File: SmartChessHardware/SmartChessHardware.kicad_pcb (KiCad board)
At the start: 2 copper layers, 294 parts, among them IC1 Pi-Zero-UART, IC2 Arduino_UNO_R3, IC3 MCP23017x-x-SO, J1 Barrel_Jack, SW200 SW_Reed, SW201 SW_Reed, SW202 SW_Reed, SW203 SW_Reed, SW204 SW_Reed, SW205 SW_Reed, SW206 SW_Reed, SW207 SW_Reed, SW208 SW_Reed, SW209 SW_Reed, SW210 SW_Reed, SW211 SW_Reed, SW212 SW_Reed, SW213 SW_Reed, SW214 SW_Reed, SW215 SW_Reed, SW216 SW_Reed, SW217 SW_Reed, SW218 SW_Reed, SW219 SW_Reed, SW220 SW_Reed, SW221 SW_Reed, SW222 SW_Reed, SW223 SW_Reed, SW224 SW_Reed, SW225 SW_Reed, SW226 SW_Reed, SW227 SW_Reed, SW228 SW_Reed, SW229 SW_Reed, SW230 SW_Reed, SW231 SW_Reed, SW232 SW_Reed, SW233 SW_Reed, SW234 SW_Reed, SW235 SW_Reed, SW236 SW_Reed, SW237 SW_Reed, SW238 SW_Reed, SW239 SW_Reed, SW240 SW_Reed, SW241 SW_Reed, SW242 SW_Reed, SW243 SW_Reed, SW244 SW_Reed, SW245 SW_Reed, SW246 SW_Reed, SW247 SW_Reed, SW248 SW_Reed, SW249 SW_Reed, SW250 SW_Reed, SW251 SW_Reed, SW252 SW_Reed, SW253 SW_Reed, SW254 SW_Reed, SW255 SW_Reed, SW256 SW_Reed, SW257 SW_Reed, SW258 SW_Reed, SW259 SW_Reed, SW260 SW_Reed, SW261 SW_Reed, SW262 SW_Reed, SW263 SW_Reed

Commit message: Placed board components
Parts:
- moved D108 368.0 mm to (302.1, 62.6)
- moved SW256 366.1 mm to (291.5, 252.5)
- moved SW216 361.2 mm to (292.0, 102.0)
- moved SW208 361.0 mm to (291.2, 72.0)
- moved D256 360.5 mm to (292.0, 260.5), turned to 90 degrees
- moved D208 360.1 mm to (291.5, 80.0), turned to 90 degrees
- moved D116 355.5 mm to (302.6, 92.2)
- moved SW240 352.2 mm to (292.5, 192.5)
- moved SW255 351.3 mm to (291.5, 222.5)
- moved SW224 351.2 mm to (293.0, 133.0)
- moved D216 350.0 mm to (292.0, 111.0), turned to 90 degrees
- moved D255 349.2 mm to (292.0, 230.5), turned to 90 degrees
- moved SW232 348.6 mm to (292.2, 164.0)
- moved D224 345.9 mm to (293.0, 139.5), turned to 90 degrees
- moved D232 344.8 mm to (292.5, 171.5), turned to 90 degrees
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
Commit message: Rearranged scanning groups
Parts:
- moved D239 211.3 mm to (293.3, 172.0)
- moved SW239 211.3 mm to (293.3, 163.5)
- moved D231 210.9 mm to (292.9, 140.1)
- moved SW231 210.9 mm to (292.4, 133.1)
- moved D223 210.2 mm to (293.2, 110.4)
- moved SW223 210.2 mm to (293.2, 102.4)
- moved D256 209.6 mm to (82.4, 261.0)
- moved SW256 209.6 mm to (81.9, 253.0)
- moved D247 209.6 mm to (293.1, 200.5)
- moved SW247 209.6 mm to (293.1, 192.5)
- moved D224 209.4 mm to (83.6, 139.9)
- moved SW224 209.4 mm to (83.6, 133.4)
- moved D263 209.2 mm to (292.2, 261.4)
- moved SW263 209.2 mm to (292.2, 252.9)
- moved D215 209.2 mm to (292.2, 82.0)
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
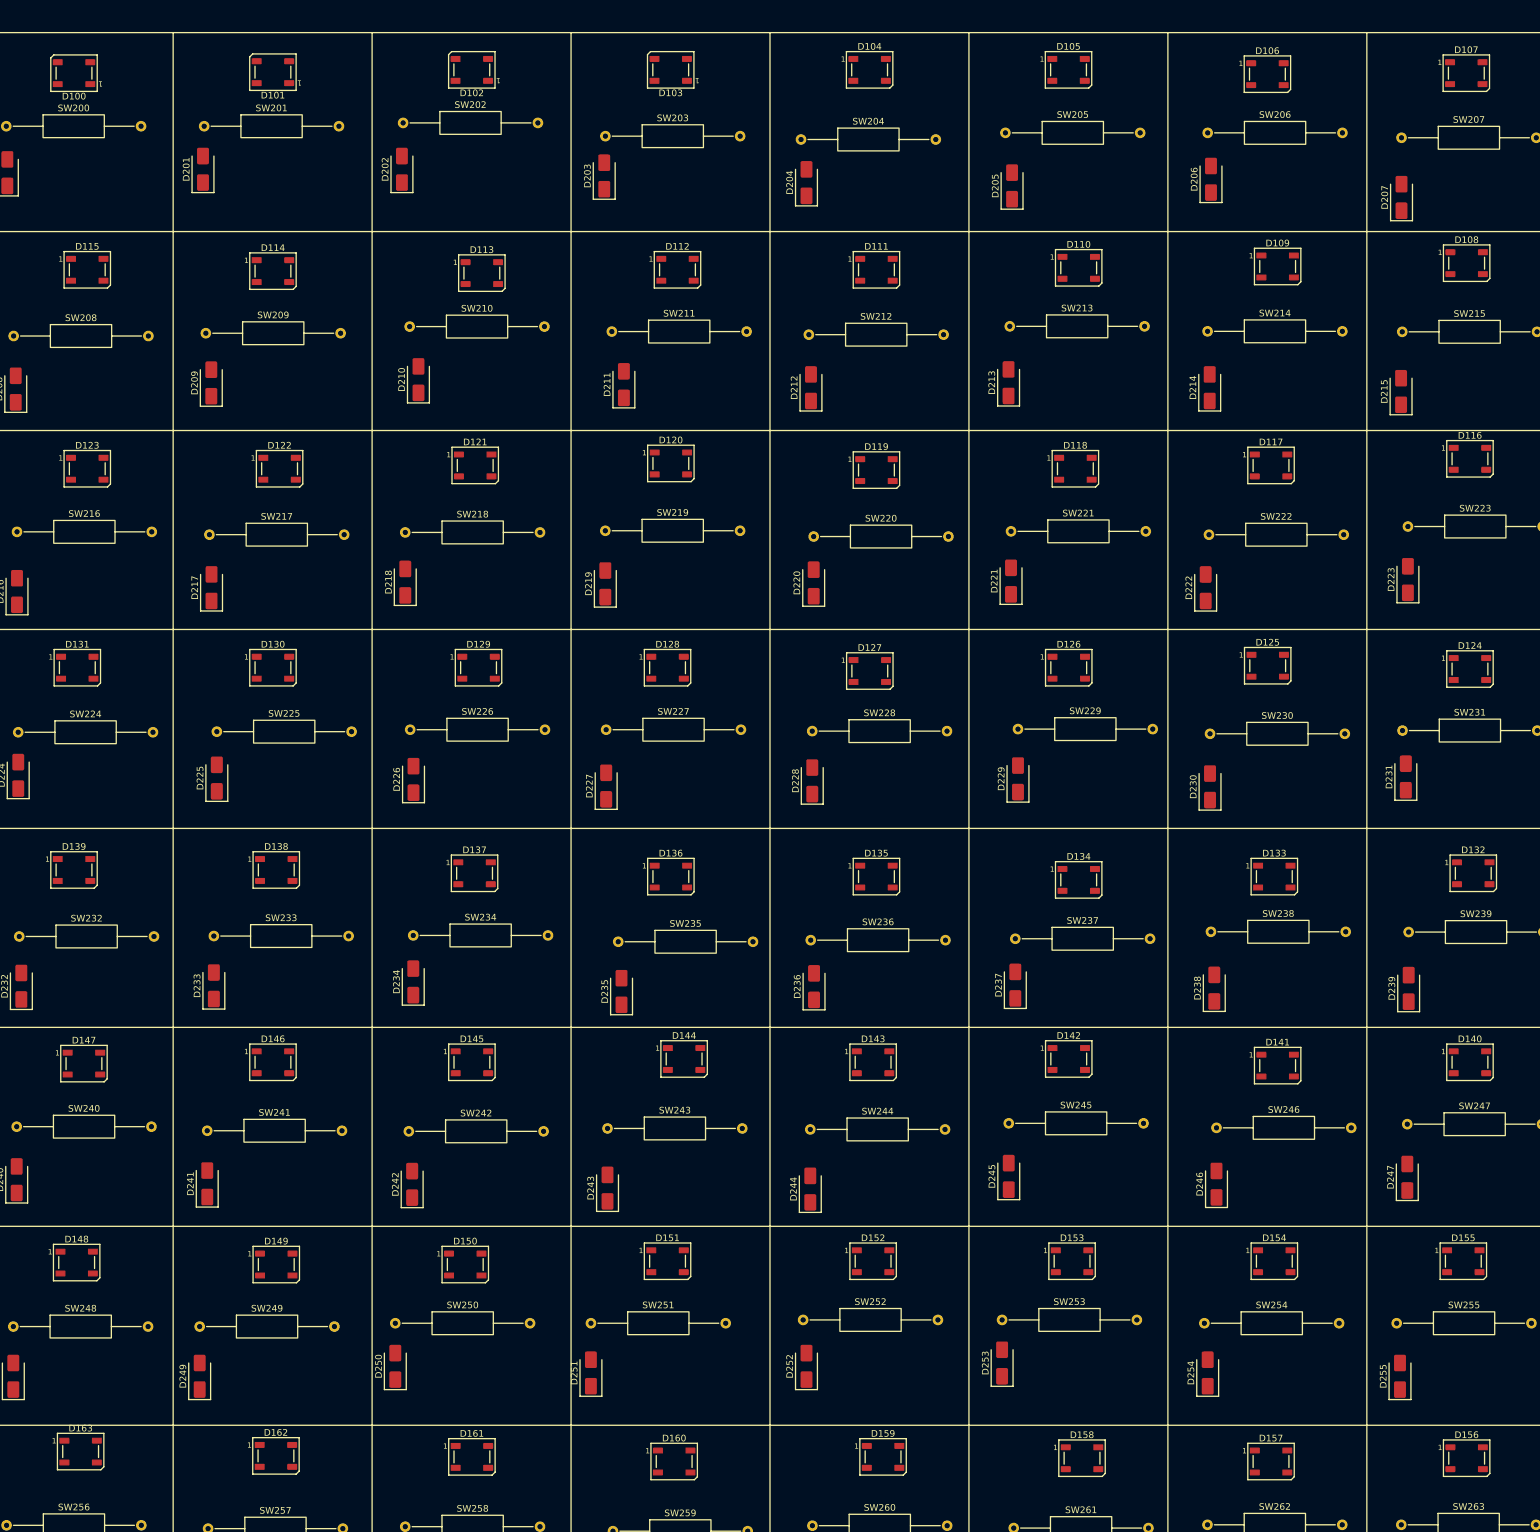
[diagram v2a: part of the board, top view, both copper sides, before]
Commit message: Fixed led placing
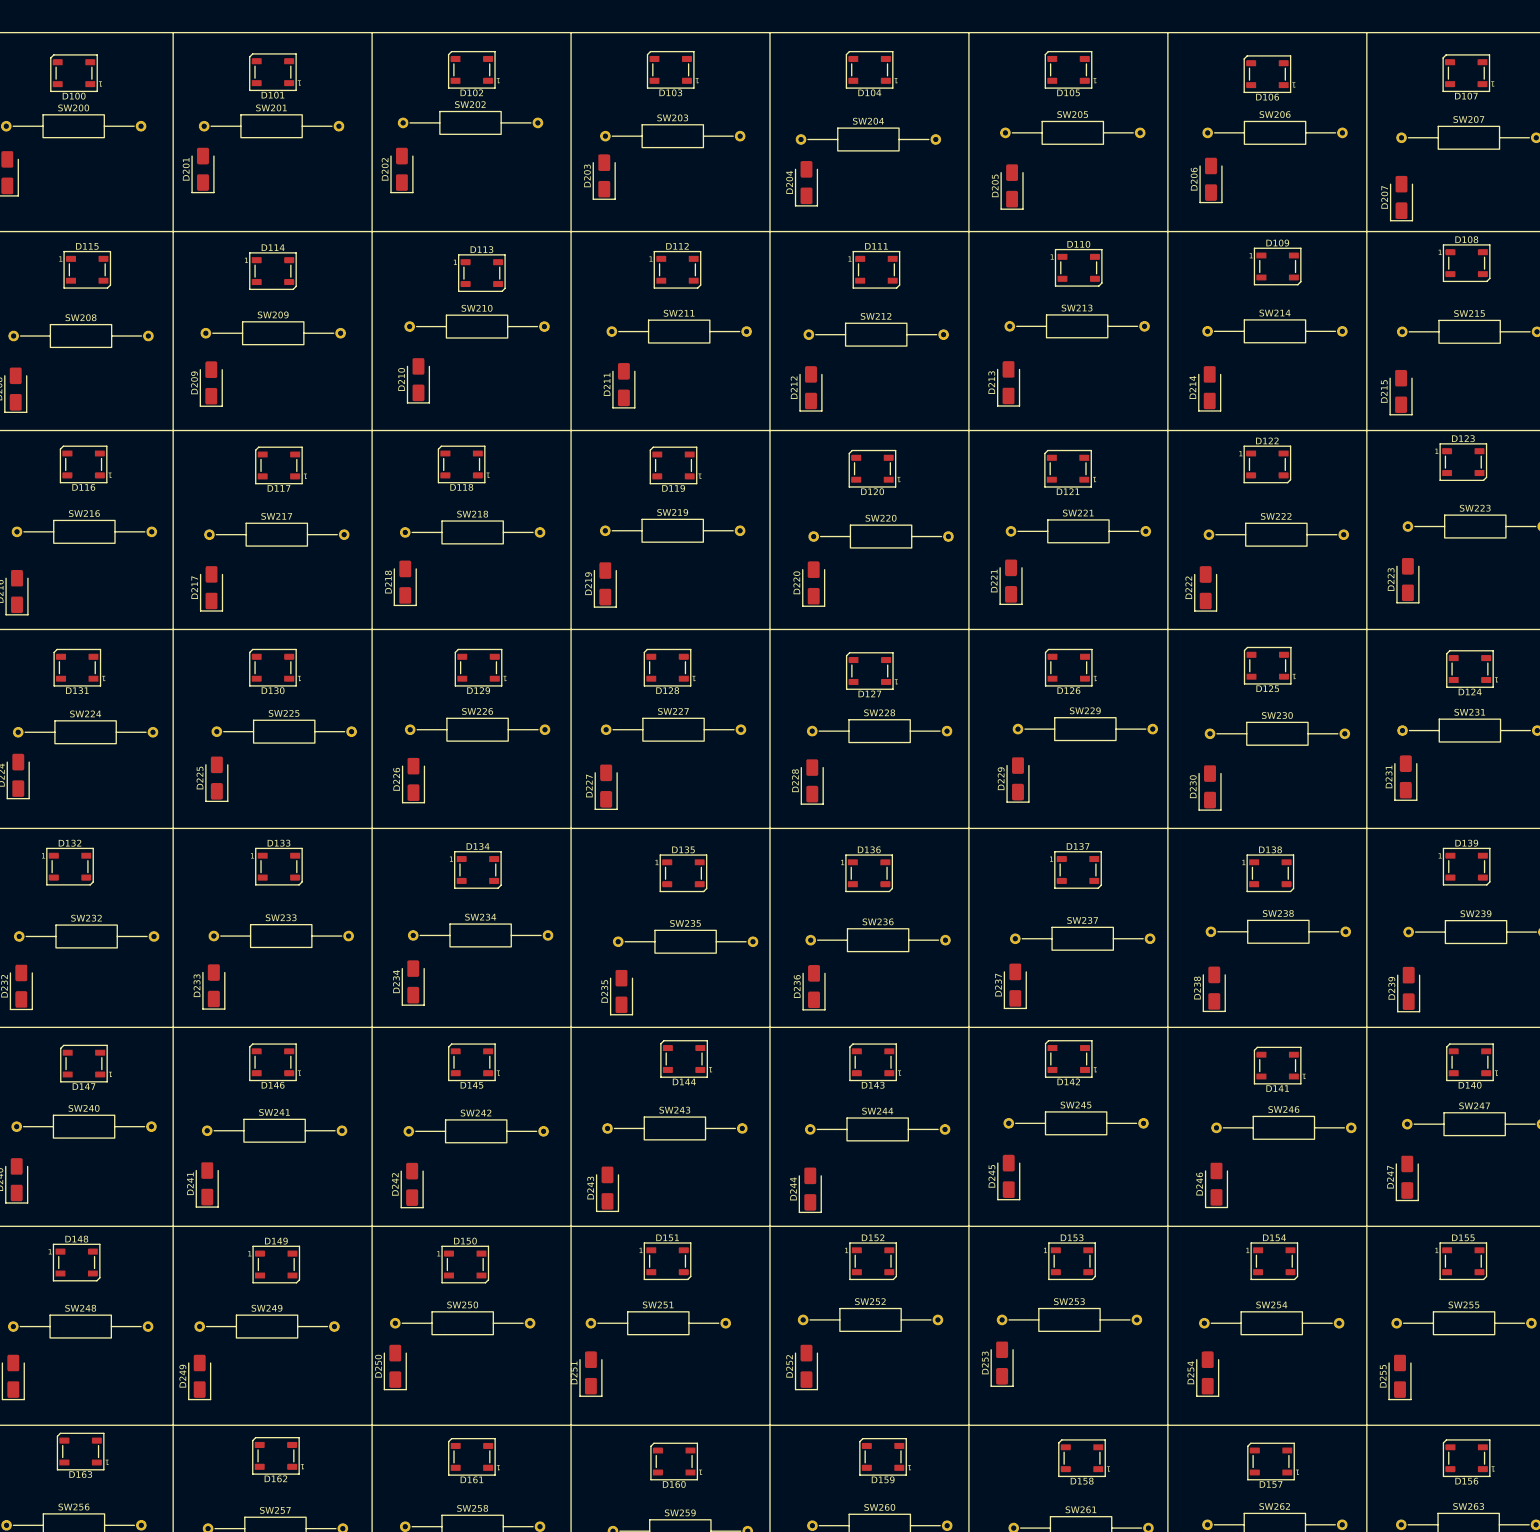
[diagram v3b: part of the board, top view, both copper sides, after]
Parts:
- moved D132 211.6 mm to (91.5, 153.7)
- moved D139 210.0 mm to (302.1, 153.7)
- moved D116 209.1 mm to (93.5, 93.0), turned to 180 degrees
- moved D123 207.5 mm to (301.6, 92.7)
- moved D133 150.1 mm to (123.0, 153.7)
- moved D138 149.9 mm to (272.4, 154.7)
- moved D117 149.6 mm to (123.0, 93.2), turned to 180 degrees
- moved D122 149.0 mm to (272.0, 93.0)
- moved D118 92.6 mm to (150.5, 93.0), turned to 180 degrees
- moved D137 91.0 mm to (243.4, 154.2)
- moved D134 90.6 mm to (152.9, 154.2)
- moved D121 89.4 mm to (241.9, 93.7), turned to 180 degrees
- moved D119 30.6 mm to (182.4, 93.2), turned to 180 degrees
- moved D120 30.4 mm to (212.4, 93.7), turned to 180 degrees
- moved D136 29.9 mm to (211.9, 154.7)
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
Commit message: Aligned LEDS
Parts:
- moved D135 2.65 mm to (181.7, 153.2)
- moved D118 2.64 mm to (152.9, 94.0)
- moved D109 2.38 mm to (271.3, 63.9)
- moved D110 2.05 mm to (241.6, 63.9)
- moved D137 1.81 mm to (241.9, 153.2)
- moved D158 1.73 mm to (242.3, 242.6)
- moved D150 1.63 mm to (152.2, 212.5)
- moved D108 1.62 mm to (301.0, 63.9)
- moved D134 1.61 mm to (151.6, 153.2)
- moved D159 1.57 mm to (212.5, 242.6)
- moved D154 1.52 mm to (271.7, 212.5)
- moved D138 1.49 mm to (272.0, 153.2)
- moved D133 1.47 mm to (121.5, 153.2)
- moved D136 1.42 mm to (211.8, 153.2)
- moved D146 1.37 mm to (123.4, 183.4)
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
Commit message: Aligned no key ghosting diodes
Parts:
- moved D216 4.68 mm to (83.1, 107.5)
- moved D262 4.42 mm to (262.5, 258.0)
- moved D222 4.10 mm to (262.9, 107.5)
- moved D217 4.10 mm to (113.1, 107.5)
- moved D207 3.74 mm to (292.2, 49.0)
- moved D219 3.60 mm to (173.0, 107.5)
- moved D220 3.43 mm to (203.0, 107.5)
- moved D218 3.41 mm to (143.0, 107.5)
- moved D263 3.40 mm to (292.5, 258.0)
- moved D235 3.38 mm to (173.0, 169.5)
- moved D260 3.31 mm to (202.6, 258.0)
- moved D261 3.14 mm to (232.5, 258.0)
- moved D221 3.12 mm to (232.9, 107.5)
- moved D211 3.03 mm to (172.7, 79.0)
- moved D215 3.00 mm to (292.0, 79.0)
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
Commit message: Placed Matrix pull up resistors
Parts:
- moved R207 336.4 mm to (311.5, 40.0)
- moved R206 306.5 mm to (281.5, 40.0)
- moved R205 276.9 mm to (251.8, 40.0)
- moved R204 246.8 mm to (221.7, 40.0)
- moved R203 216.9 mm to (191.5, 40.0)
- moved R202 187.3 mm to (161.5, 39.5)
- moved R201 157.5 mm to (131.5, 40.0)
- moved R200 135.9 mm to (101.3, 40.0)
- renumbered R207 to R200, R200 to R201, R201 to R202, R202 to R203, R203 to R204, R204 to R205, R205 to R206, R206 to R207

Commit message: Fixed wrong placed diodes
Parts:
- turned D124 to 0 degrees
- turned D125 to 0 degrees
- turned D126 to 0 degrees
- turned D127 to 0 degrees
- turned D128 to 0 degrees
- turned D129 to 0 degrees
- turned D130 to 0 degrees
- turned D131 to 0 degrees
- turned D132 to 180 degrees
- turned D133 to 180 degrees
- turned D134 to 180 degrees
- turned D135 to 180 degrees
- turned D136 to 180 degrees
- turned D137 to 180 degrees
- turned D138 to 180 degrees
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
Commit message: Placed filtering capacitors for leds
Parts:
- C114: footprint Capacitor_SMD:C_0603_1608Metric -> Capacitor_THT:CP_Radial_D6.3mm_P2.50mm; moved to B.Cu
- moved C106 410.3 mm to (306.5, 37.5), turned to 90 degrees
- moved C107 393.2 mm to (296.5, 60.0), turned to -90 degrees
- moved C105 382.1 mm to (276.5, 37.2), turned to 90 degrees
- moved C124 379.1 mm to (306.0, 96.5), turned to -90 degrees
- moved C108 367.1 mm to (267.0, 60.0), turned to -90 degrees
- moved C125 366.1 mm to (298.0, 121.5), turned to 90 degrees
- moved C139 365.9 mm to (306.5, 156.0), turned to 90 degrees
- moved C140 355.1 mm to (298.0, 181.0), turned to -90 degrees
- moved C156 354.9 mm to (306.0, 215.0), turned to -90 degrees
- moved C104 354.0 mm to (246.5, 37.5), turned to 90 degrees
- moved C123 350.0 mm to (276.5, 96.5), turned to -90 degrees
- moved C157 348.6 mm to (297.5, 240.0), turned to 90 degrees
- moved C109 341.0 mm to (237.0, 60.0), turned to -90 degrees
- moved C126 337.3 mm to (268.0, 121.5), turned to 90 degrees
- moved C138 335.8 mm to (276.5, 156.0), turned to 90 degrees
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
